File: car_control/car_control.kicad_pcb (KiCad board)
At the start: 2 copper layers, 179.7 x 101.6 mm, 31 parts, among them J1 Screw_Terminal_01x02, J2 Conn_01x03, J3 Conn_01x03, J4 Screw_Terminal_01x02, J5 Conn_01x06, Q1 IRF540N, Q2 2N3904, SW1 SW_SPST, SW2 SW_Push, U1 TCRT5000

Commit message: Right angle 10mm headlights/tail lights
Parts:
- removed REF**: car_as, car_as:car_as
- added N2: Housing, car_as:car_as, F.Cu at (107.4, 5.71)
- D4, D5: value LED -> LED_White_10mm; footprint LED_THT:LED_D3.0mm_Horizontal_O3.81mm_Z2.0mm -> my_10mm_led:LED_D10.0mm_white
- D6, D7: value LED -> LED_Red_10mm; footprint LED_THT:LED_D3.0mm_Horizontal_O3.81mm_Z2.0mm -> my_10mm_led:LED_D10.0mm_red
- R1: value 999 -> 150
- R2: value 999 -> 240
- R3, R4: value 999 -> 200
- R5, R6: value 999 -> 330

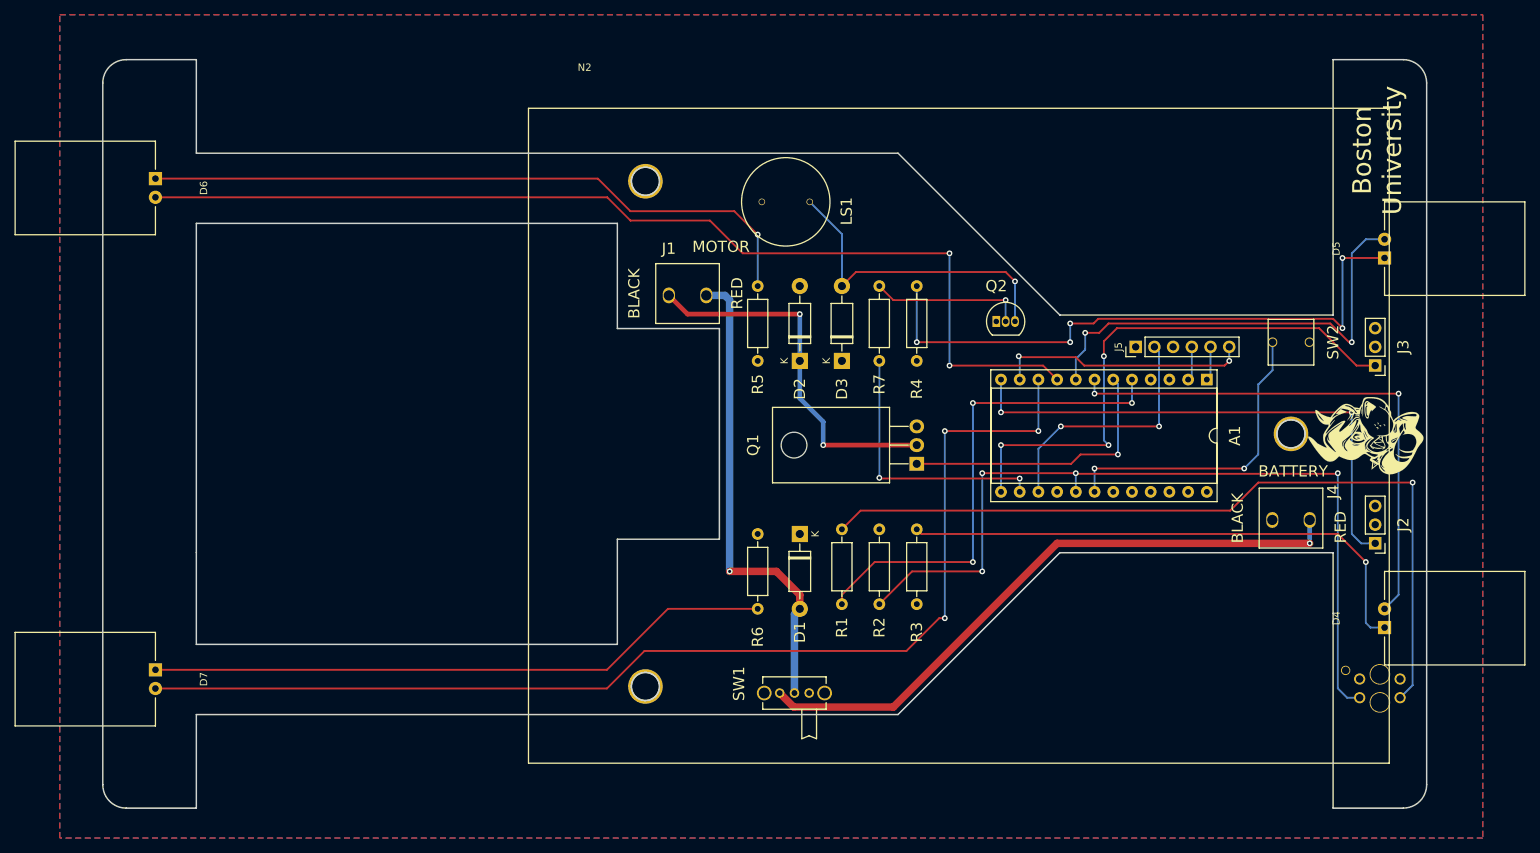
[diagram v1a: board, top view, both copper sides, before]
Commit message: New board outline, LEDs need fixing
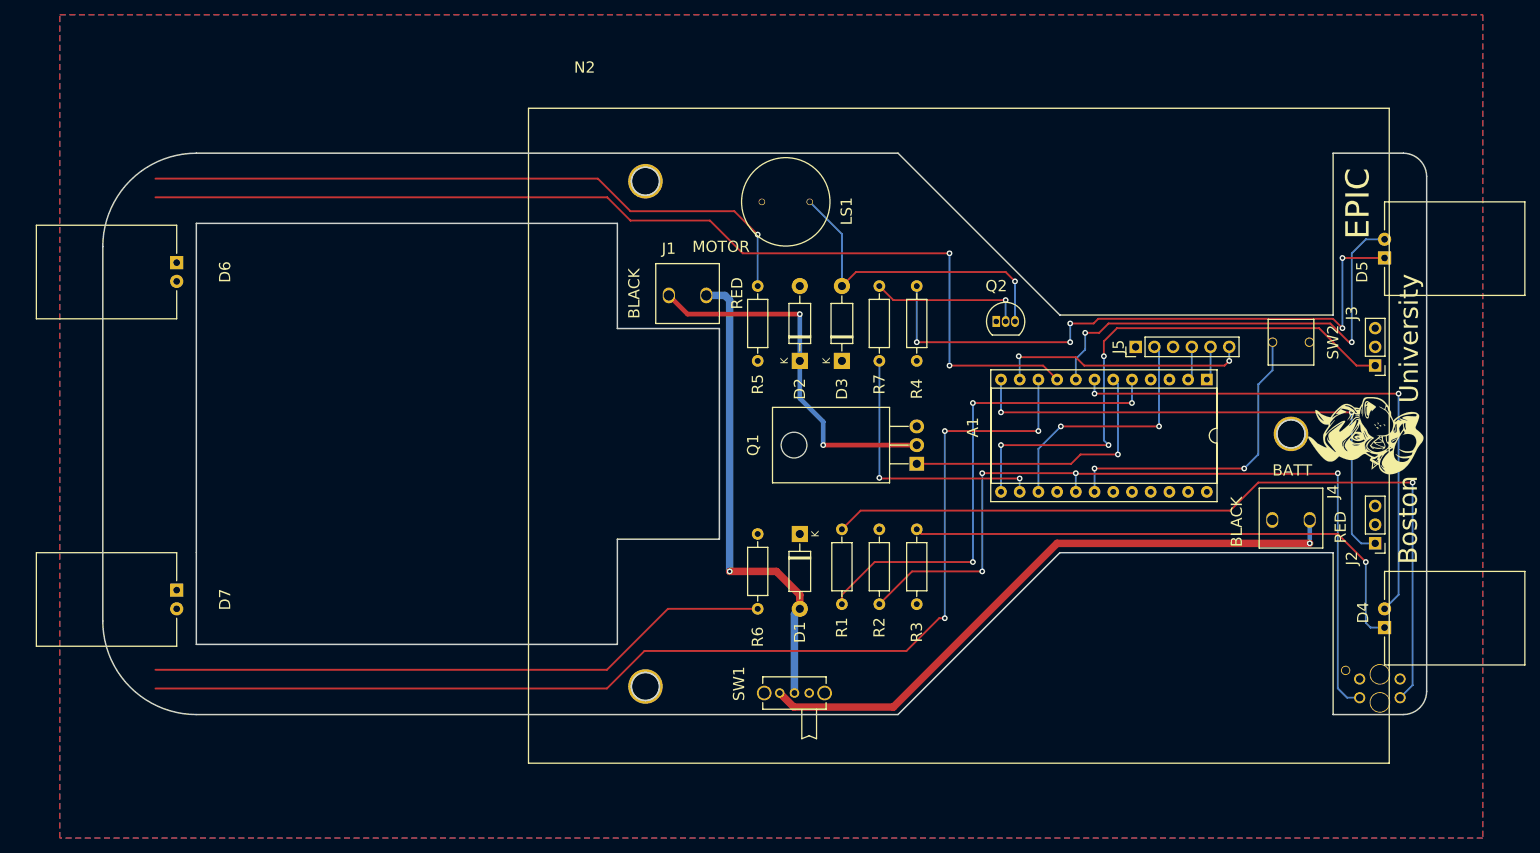
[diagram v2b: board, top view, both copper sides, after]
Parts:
- moved D6 11.8 mm to (82.5, 64.8)
- moved D7 11.2 mm to (82.5, 109.2)
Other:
- board size 179.7 x 101.6 mm -> 179.7 x 76.2 mm
- board text added: "BATT"
- board text added: "Boston"
- board text added: "EPIC"
- board text added: "University"
- board text removed: "BATTERY"
- board text removed: "Boston University"

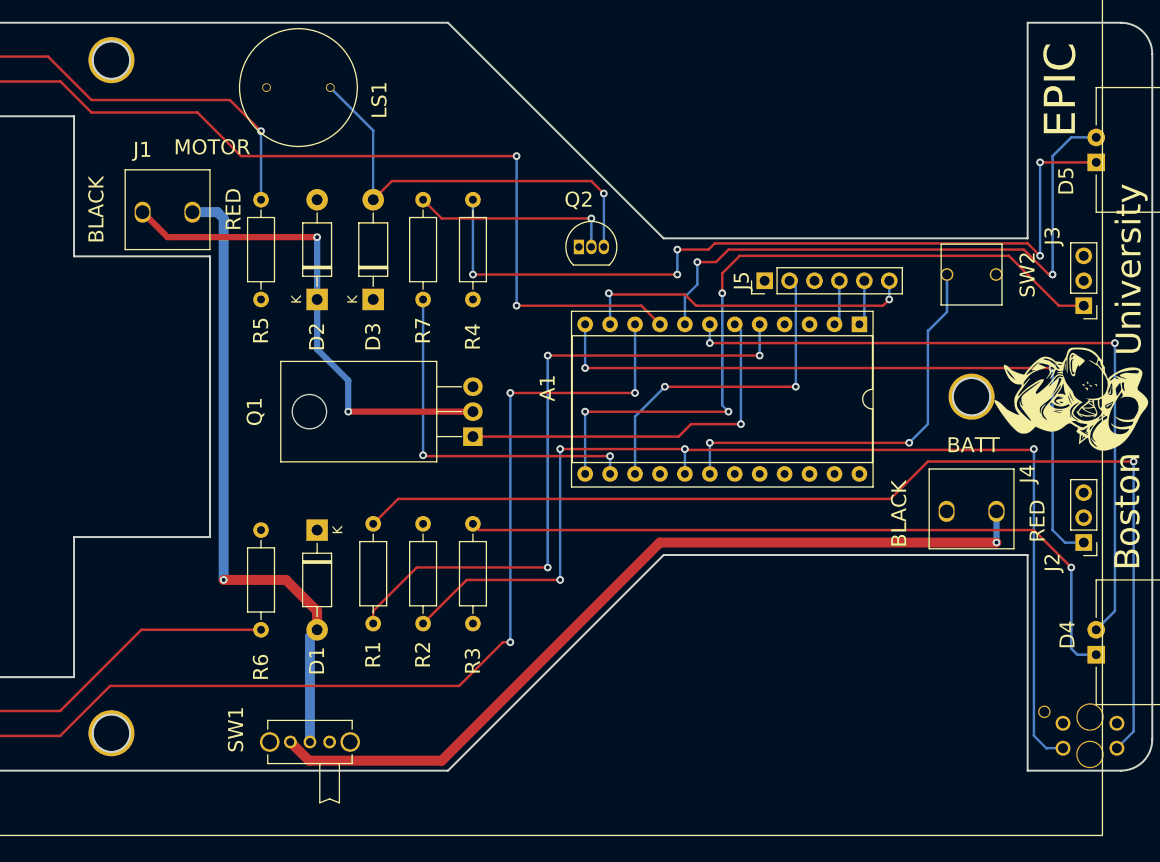
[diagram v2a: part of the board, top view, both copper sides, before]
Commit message: add cherry switch, change pwr sw to header, reroute
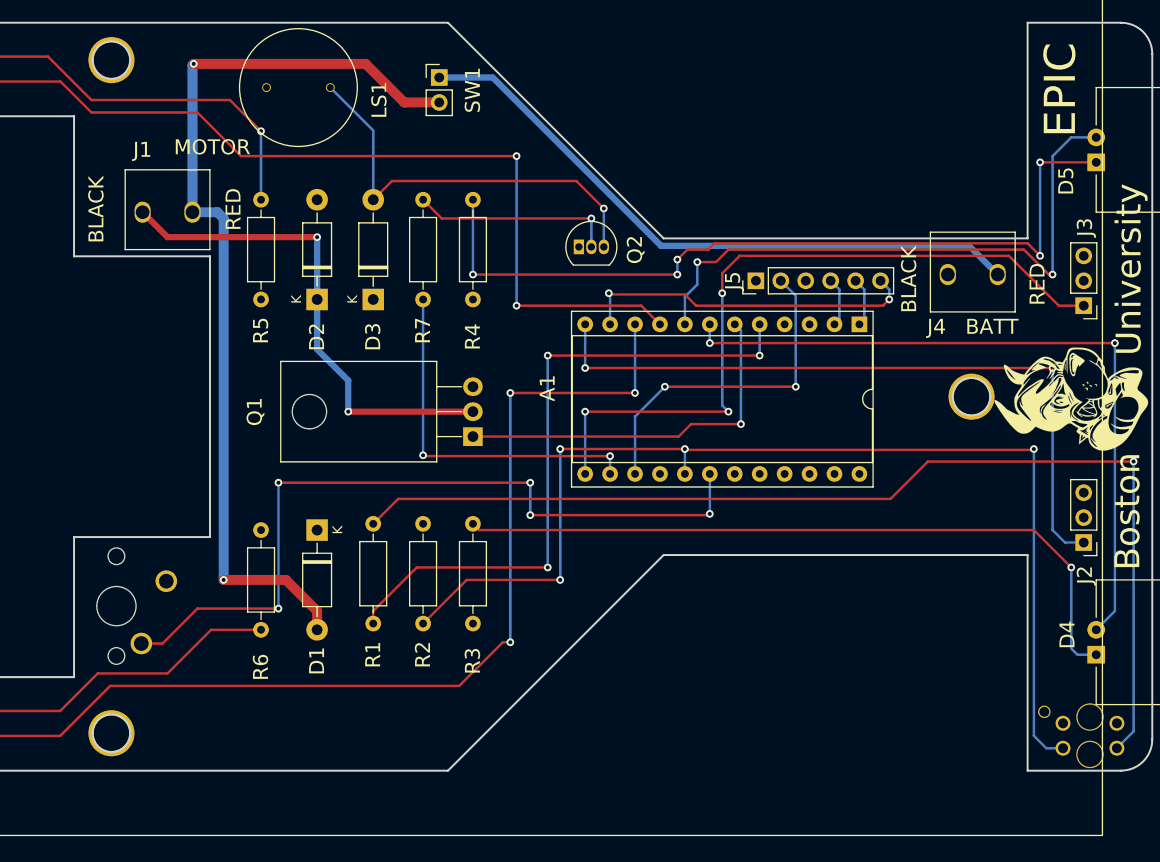
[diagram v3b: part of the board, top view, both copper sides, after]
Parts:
- SW1: footprint mini_slide_switch:OS102011MA1QN1 -> Connector_PinHeader_2.54mm:PinHeader_1x02_P2.54mm_Vertical
- SW2: footprint my_pushbutton:sw_push_6.2x6.2mm_p5 -> my_cherry:SW_Cherry_MX_1.00u_PCB; moved to B.Cu
- moved SW2 87.8 mm to (151.8, 106.8), turned to 90 degrees
- moved SW1 69.0 mm to (179.6, 55.5)
- moved J4 24.1 mm to (233.9, 75.6)
- moved J5 0.89 mm to (211.8, 76.2)
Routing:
- net Net-(A1-A1): track 42.3 -> 79.6 mm, vias 2 -> 5
- net Net-(D1-A): track 64.7 -> 94.8 mm, vias 1 -> 2
- net Net-(J4-Pin_1): track 85.1 -> 65.2 mm, vias 1 -> 0
- net Net-(D3-A): track 43.5 -> 42.6 mm
- net Net-(D5-K): track 84.0 -> 83.4 mm

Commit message: Rev 1 as built
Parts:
- removed N2: Housing, car_as:car_as
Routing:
- net Net-(D6-K): track 91.9 -> 123.2 mm
- net Net-(A1-D7): track 156.2 -> 186.7 mm
- net Net-(A1-D6): track 141.6 -> 157.9 mm
- net Net-(D7-K): track 85.2 -> 98.1 mm
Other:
- outline, holes or cut-outs redrawn
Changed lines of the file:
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@@
     (pad_to_mask_clearance 0)
     (pcbplotparams
-      (layerselection 0x00010fc_ffffffff)
+      (layerselection 0x00010f0_ffffffff)
       (plot_on_all_layers_selection 0x0000000_00000000)
       (disableapertmacros false)
@@
       (outputformat 1)
       (mirror false)
-      (drillshape 1)
+      (drillshape 0)
       (scaleselection 1)
-      (outputdirectory "")
+      (outputdirectory "gerber/")
     )
   )
@@
     )
   )
-  (footprint "car_as:car_as" (layer "F.Cu")
-    (at 107.443 5.713)
-    (property "Sheetfile" "car_control.kicad_sch")
-    (property "Sheetname" "")
-    (property "ki_description" "Housing")
-    (property "ki_keywords" "housing enclosure")
-    (fp_text reference "N2" (at 30.48 32.56 unlocked) (layer "F.SilkS")
-        (effects (font (size 1.524 1.524) (thickness 0.2032)))
-    )
-    (fp_text value "Housing" (at 30.48 34.06 unlocked) (layer "F.Fab")
-        (effects (font (size 1 1) (thickness 0.15)))
-    )
-    (fp_text user "${REFERENCE}" (at 30.48 35.56 unlocked) (layer "F.Fab")
-        (effects (font (size 1 1) (thickness 0.15)))
-    )
-    (fp_line (start 22.86 38.1) (end 139.7 38.1)
-      (stroke (width 0.1) (type default)) (layer "F.SilkS"))
-    (fp_line (start 22.86 127) (end 22.86 38.1)
-      (stroke (width 0.1) (type default)) (layer "F.SilkS"))
-    (fp_line (start 139.7 38.1) (end 139.7 127)
-      (stroke (width 0.1) (type default)) (layer "F.SilkS"))
-    (fp_line (start 139.7 127) (end 22.86 127)
-      (stroke (width 0.1) (type default)) (layer "F.SilkS"))
-    (pad "" np_thru_hole circle (at 38.735 48.006) (size 3.81 3.81) (drill 3.81) (layers "F&B.Cu" "*.Mask"))
-    (pad "" np_thru_hole circle (at 38.735 116.586) (size 3.81 3.81) (drill 3.81) (layers "F&B.Cu" "*.Mask"))
-    (pad "" np_thru_hole circle (at 126.365 82.296) (size 3.81 3.81) (drill 3.81) (layers "F&B.Cu" "*.Mask"))
-    (model "/home/hazen/work/epic-car-control/mech/car_as_footprint.wrl"
-      (offset (xyz 64.135 -82.55 -24.765))
-      (scale (xyz 10 10 10))
-      (rotate (xyz 0 0 0))
-    )
-  )
   (footprint "Package_TO_SOT_THT:TO-220-3_Horizontal_TabDown" (layer "F.Cu")
     (at 183.008 92.075 90)
@@
   (gr_line (start 142.367 102.3112) (end 156.218371 102.3112)
     (stroke (width 0.2) (type solid)) (layer "Edge.Cuts"))
-  (gr_circle (center 146.177 122.301) (end 148.082 122.301)
-    (stroke (width 0.2) (type solid)) (fill none) (layer "Edge.Cuts"))
   (gr_line (start 239.522 104.142) (end 239.522 126.111)
     (stroke (width 0.2) (type solid)) (layer "Edge.Cuts"))
@@
   (gr_arc (start 85.217002 126.111) (mid 76.236744 122.391257) (end 72.517 113.411)
     (stroke (width 0.2) (type solid)) (layer "Edge.Cuts"))
-  (gr_circle (center 233.807 88.011) (end 235.712 88.011)
-    (stroke (width 0.2) (type solid)) (fill none) (layer "Edge.Cuts"))
   (gr_line (start 180.467 49.911) (end 202.436 71.88)
     (stroke (width 0.2) (type solid)) (layer "Edge.Cuts"))
@@
   (gr_line (start 239.522 49.911) (end 239.522 71.88)
     (stroke (width 0.2) (type solid)) (layer "Edge.Cuts"))
-  (gr_circle (center 146.177 53.721) (end 148.082 53.721)
-    (stroke (width 0.2) (type solid)) (fill none) (layer "Edge.Cuts"))
   (gr_line (start 180.467 126.111) (end 202.436 104.142)
     (stroke (width 0.2) (type solid)) (layer "Edge.Cuts"))
@@
     (effects (font (size 1.524 1.524) (thickness 0.2032)) (justify left bottom))
   )
-  (dimension (type orthogonal) (layer "Dwgs.User")
-    (pts (xy 142.368 49.909) (xy 239.523 37.209))
-    (height -16.254)
-    (orientation 0)
-    (gr_text "3.8250 in" (at 190.9455 32.505) (layer "Dwgs.User")
-      (effects (font (size 1 1) (thickness 0.15)))
-    )
-    (format (prefix "") (suffix "") (units 3) (units_format 1) (precision 4))
-    (style (thickness 0.15) (arrow_length 1.27) (text_position_mode 0) (extension_height 0.58642) (extension_offset 0.5) keep_text_aligned)
-  )
   (segment (start 221.996 76.2) (end 222.885 77.089) (width 0.254) (layer "B.Cu") (net 1))
   (segment (start 222.885 80.138) (end 222.383 80.64) (width 0.254) (layer "B.Cu") (net 1))
@@
   (segment (start 154.94 59.055) (end 159.385 63.5) (width 0.254) (layer "F.Cu") (net 8))
   (segment (start 187.453 78.74) (end 200.163 78.74) (width 0.254) (layer "F.Cu") (net 8))
+  (segment (start 77.47 58.095) (end 79.665 55.9) (width 0.254) (layer "F.Cu") (net 8))
   (segment (start 200.163 78.74) (end 202.063 80.64) (width 0.254) (layer "F.Cu") (net 8))
   (segment (start 140.99 55.9) (end 144.145 59.055) (width 0.254) (layer "F.Cu") (net 8))
+  (segment (start 79.375 67.31) (end 77.47 65.405) (width 0.254) (layer "F.Cu") (net 8))
   (segment (start 79.665 55.9) (end 140.99 55.9) (width 0.254) (layer "F.Cu") (net 8))
+  (segment (start 82.55 67.31) (end 79.375 67.31) (width 0.254) (layer "F.Cu") (net 8))
+  (segment (start 77.47 65.405) (end 77.47 58.095) (width 0.254) (layer "F.Cu") (net 8))
   (via (at 187.453 63.5) (size 0.7874) (drill 0.4064) (layers "F.Cu" "B.Cu") (net 8))
   (via (at 187.453 78.74) (size 0.7874) (drill 0.4064) (layers "F.Cu" "B.Cu") (net 8))
   (segment (start 187.453 63.5) (end 187.453 78.74) (width 0.254) (layer "B.Cu") (net 8))
-  (segment (start 181.61 117.475) (end 186.055 113.03) (width 0.254) (layer "F.Cu") (net 9))
-  (segment (start 186.818 87.63) (end 199.518 87.63) (width 0.254) (layer "F.Cu") (net 9))
-  (segment (start 79.665 122.575) (end 140.95 122.575) (width 0.254) (layer "F.Cu") (net 9))
   (segment (start 140.95 122.575) (end 146.05 117.475) (width 0.254) (layer "F.Cu") (net 9))
+  (segment (start 186.818 87.63) (end 199.518 87.63) (width 0.254) (layer "F.Cu") (net 9))
+  (segment (start 77.851 106.426) (end 77.343 106.934) (width 0.254) (layer "F.Cu") (net 9))
+  (segment (start 84.455 111.379) (end 84.455 107.188) (width 0.254) (layer "F.Cu") (net 9))
+  (segment (start 77.343 120.142) (end 79.665 122.464) (width 0.254) (layer "F.Cu") (net 9))
   (segment (start 146.05 117.475) (end 181.61 117.475) (width 0.254) (layer "F.Cu") (net 9))
+  (segment (start 84.074 111.76) (end 84.455 111.379) (width 0.254) (layer "F.Cu") (net 9))
+  (segment (start 84.455 107.188) (end 83.693 106.426) (width 0.254) (layer "F.Cu") (net 9))
+  (segment (start 79.665 122.575) (end 140.95 122.575) (width 0.254) (layer "F.Cu") (net 9))
+  (segment (start 77.343 106.934) (end 77.343 120.142) (width 0.254) (layer "F.Cu") (net 9))
+  (segment (start 181.61 117.475) (end 186.055 113.03) (width 0.254) (layer "F.Cu") (net 9))
+  (segment (start 79.665 122.464) (end 79.665 122.575) (width 0.254) (layer "F.Cu") (net 9))
+  (segment (start 83.693 106.426) (end 77.851 106.426) (width 0.254) (layer "F.Cu") (net 9))
+  (segment (start 82.55 111.76) (end 84.074 111.76) (width 0.254) (layer "F.Cu") (net 9))
   (segment (start 186.055 113.03) (end 186.818 113.03) (width 0.254) (layer "F.Cu") (net 9))
   (via (at 186.818 113.03) (size 0.7874) (drill 0.4064) (layers "F.Cu" "B.Cu") (net 9))
@@
   (segment (start 183.008 67.945) (end 183.008 75.565) (width 0.254) (layer "B.Cu") (net 23))
   (segment (start 240.793 73.66) (end 240.793 64.135) (width 0.254) (layer "B.Cu") (net 23))
+  (segment (start 76.962 69.342) (end 74.93 67.31) (width 0.254) (layer "F.Cu") (net 24))
+  (segment (start 83.82 69.342) (end 76.962 69.342) (width 0.254) (layer "F.Cu") (net 24))
+  (segment (start 74.93 67.31) (end 74.93 58.095) (width 0.254) (layer "F.Cu") (net 24))
   (segment (start 158.243 57.785) (end 161.418 60.96) (width 0.254) (layer "F.Cu") (net 24))
   (segment (start 139.72 53.36) (end 144.145 57.785) (width 0.254) (layer "F.Cu") (net 24))
+  (segment (start 74.93 58.095) (end 79.665 53.36) (width 0.254) (layer "F.Cu") (net 24))
   (segment (start 79.665 53.36) (end 139.72 53.36) (width 0.254) (layer "F.Cu") (net 24))
+  (segment (start 84.455 66.675) (end 84.455 68.707) (width 0.254) (layer "F.Cu") (net 24))
+  (segment (start 84.455 68.707) (end 83.82 69.342) (width 0.254) (layer "F.Cu") (net 24))
+  (segment (start 82.55 64.77) (end 84.455 66.675) (width 0.254) (layer "F.Cu") (net 24))
   (segment (start 144.145 57.785) (end 158.243 57.785) (width 0.254) (layer "F.Cu") (net 24))
   (via (at 161.418 60.96) (size 0.7874) (drill 0.4064) (layers "F.Cu" "B.Cu") (net 24))
   (segment (start 161.418 60.96) (end 161.418 67.945) (width 0.254) (layer "B.Cu") (net 24))
-  (segment (start 140.95 120.035) (end 144.78 116.205) (width 0.254) (layer "F.Cu") (net 25))
-  (segment (start 151.892 116.205) (end 156.337 111.76) (width 0.254) (layer "F.Cu") (net 25))
+  (segment (start 78.613 113.157) (end 78.613 118.983) (width 0.254) (layer "F.Cu") (net 25))
   (segment (start 156.337 111.76) (end 161.418 111.76) (width 0.254) (layer "F.Cu") (net 25))
-  (segment (start 144.78 116.205) (end 151.892 116.205) (width 0.254) (layer "F.Cu") (net 25))
+  (segment (start 82.55 109.22) (end 78.613 113.157) (width 0.254) (layer "F.Cu") (net 25))
+  (segment (start 78.613 118.983) (end 79.665 120.035) (width 0.254) (layer "F.Cu") (net 25))
+  (segment (start 151.892 116.205) (end 156.337 111.76) (width 0.254) (layer "F.Cu") (net 25))
+  (segment (start 140.95 120.035) (end 144.78 116.205) (width 0.254) (layer "F.Cu") (net 25))
   (segment (start 79.665 120.035) (end 140.95 120.035) (width 0.254) (layer "F.Cu") (net 25))
+  (segment (start 144.78 116.205) (end 151.892 116.205) (width 0.254) (layer "F.Cu") (net 25))
   (segment (start 174.753 66.04) (end 172.848 67.945) (width 0.254) (layer "F.Cu") (net 26))
   (segment (start 193.549 66.04) (end 174.753 66.04) (width 0.254) (layer "F.Cu") (net 26))
